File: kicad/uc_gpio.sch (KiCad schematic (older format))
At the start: 1 part, among them U1_? TMS320F28388DZWTS

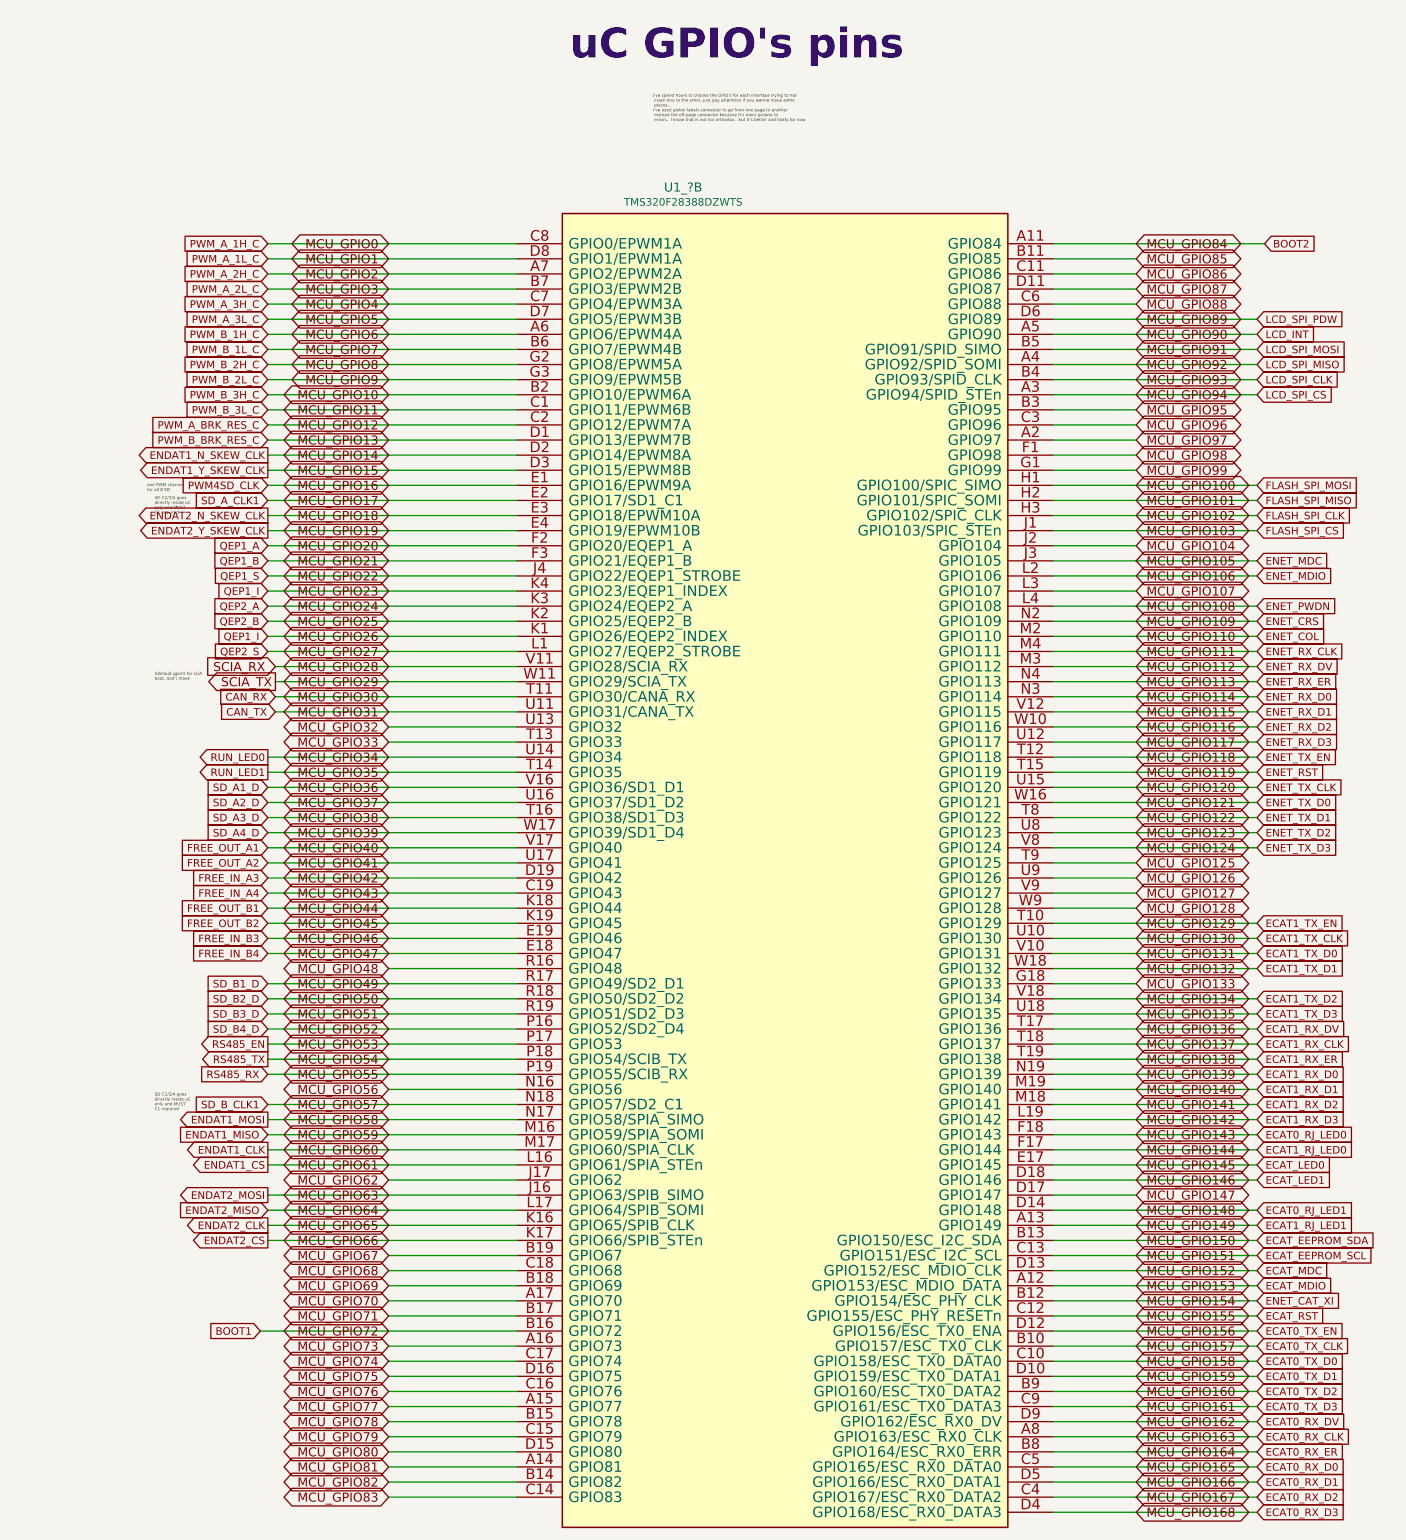
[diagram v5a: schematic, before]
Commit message: added 4 push buttons and more gpios on LCD connector
just to have more UI options. With those I'd manage graphics LCD plus 4
buttons, and charaveter LCD. or the embedded EVE graphic LCD
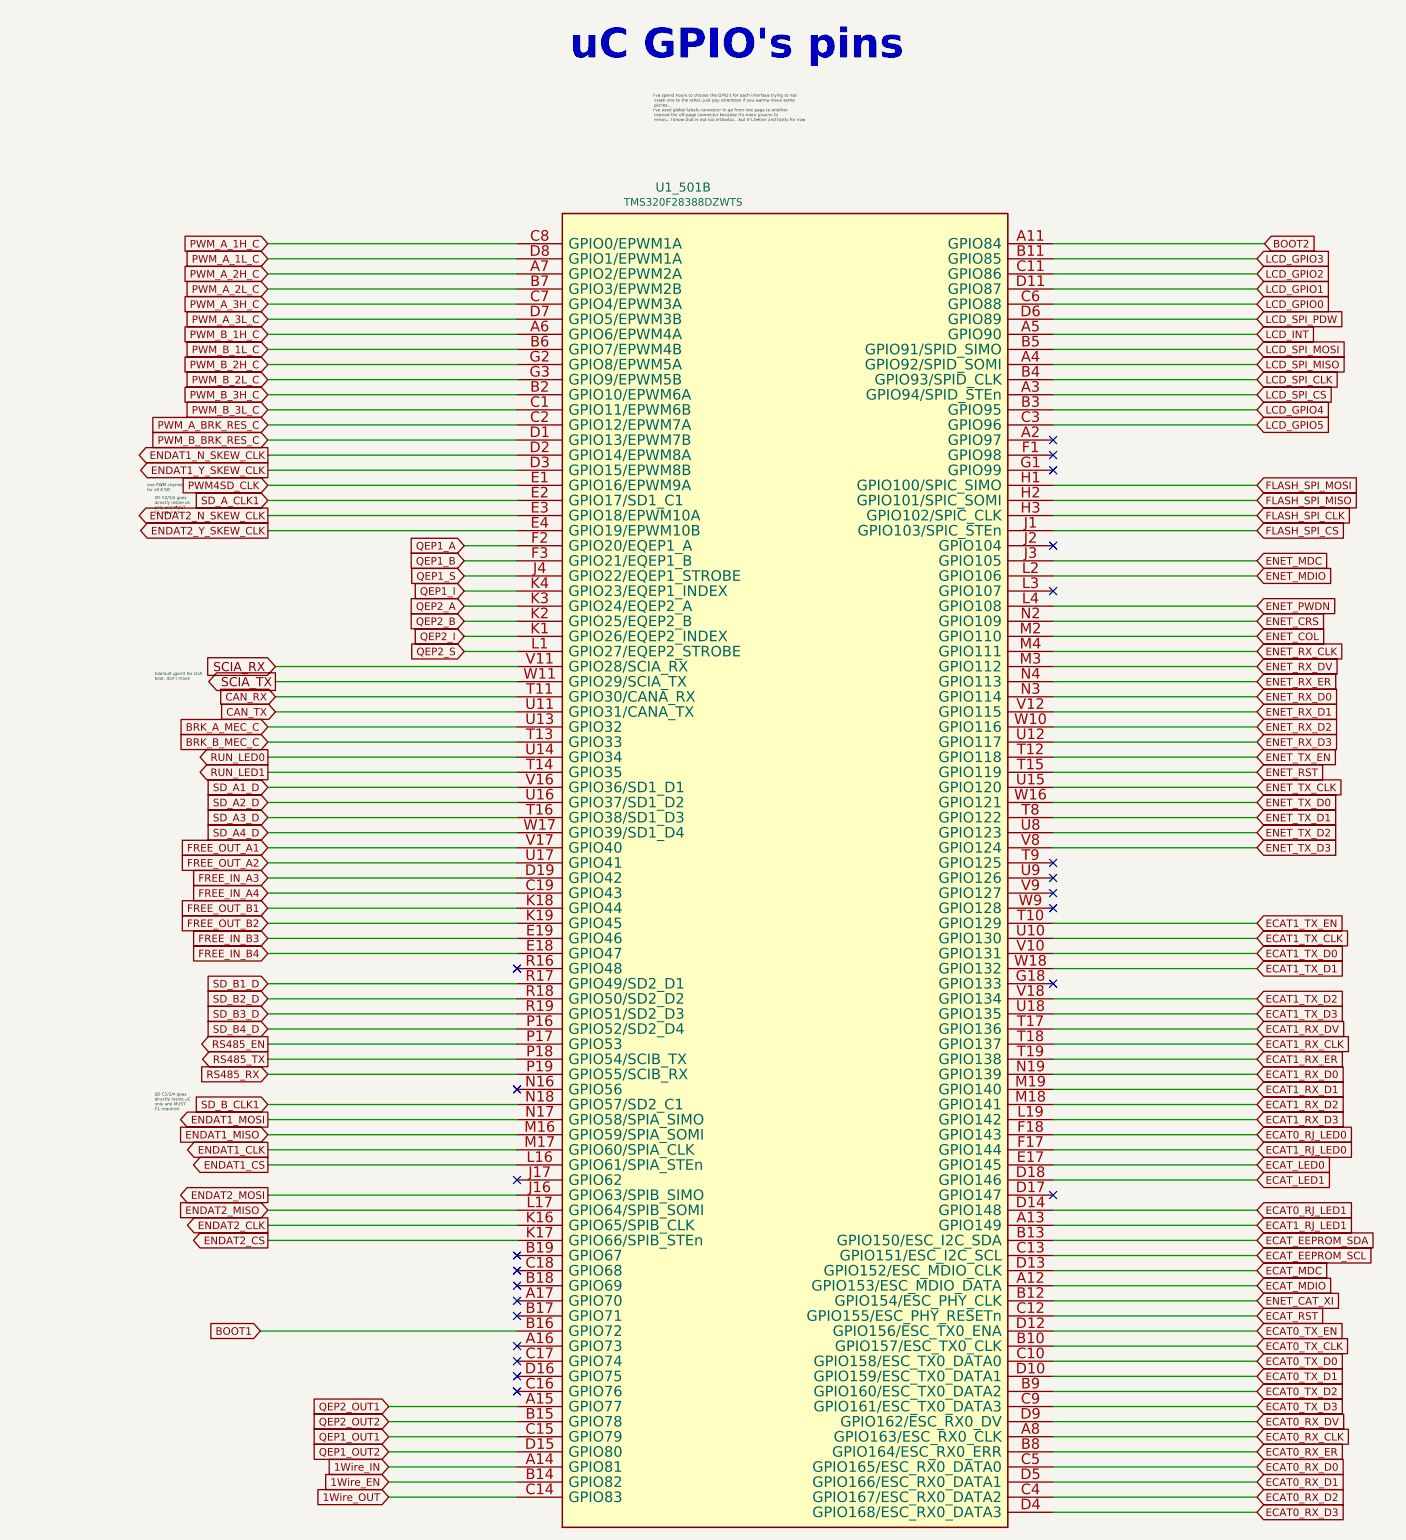
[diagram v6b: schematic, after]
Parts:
- gave numbers to parts that had none: 1
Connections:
- net MCU_GPIO0 renamed PWM_A_1H_C
- net MCU_GPIO1 renamed PWM_A_1L_C
- net MCU_GPIO10 renamed PWM_B_3H_C
- net MCU_GPIO104: no longer names the net of U1_501.J2 (GPIO104)
- net MCU_GPIO107: no longer names the net of U1_501.L3 (GPIO107)
- net MCU_GPIO11 renamed PWM_B_3L_C
- net MCU_GPIO12 renamed PWM_A_BRK_RES_C
- net MCU_GPIO125: no longer names the net of U1_501.T9 (GPIO125)
- net MCU_GPIO126: no longer names the net of U1_501.U9 (GPIO126)
- net MCU_GPIO127: no longer names the net of U1_501.V9 (GPIO127)
- net MCU_GPIO128: no longer names the net of U1_501.W9 (GPIO128)
- net MCU_GPIO13 renamed PWM_B_BRK_RES_C
- net MCU_GPIO133: no longer names the net of U1_501.G18 (GPIO133)
- net MCU_GPIO147: no longer names the net of U1_501.D17 (GPIO147)
- net MCU_GPIO16 renamed PWM4SD_CLK
- net MCU_GPIO17 renamed SD_A_CLK1
- net MCU_GPIO2 renamed PWM_A_2H_C
- net MCU_GPIO20 renamed QEP1_A
- net MCU_GPIO21 renamed QEP1_B
- net MCU_GPIO22 renamed QEP1_S
- net MCU_GPIO23 renamed QEP1_I
- net QEP1_I: no longer U1_501.K1 (GPIO26/EQEP2_INDEX)
- net MCU_GPIO24 renamed QEP2_A
- net MCU_GPIO25 renamed QEP2_B
- net MCU_GPIO27 renamed QEP2_S
- net MCU_GPIO28 renamed SCIA_RX
- net MCU_GPIO29 renamed SCIA_TX
- net MCU_GPIO3 renamed PWM_A_2L_C
- net MCU_GPIO32 renamed BRK_A_MEC_C
- net MCU_GPIO33 renamed BRK_B_MEC_C
- net MCU_GPIO34 renamed RUN_LED0
- net MCU_GPIO35 renamed RUN_LED1
- net MCU_GPIO36 renamed SD_A1_D
- net MCU_GPIO37 renamed SD_A2_D
- net MCU_GPIO38 renamed SD_A3_D
- net MCU_GPIO39 renamed SD_A4_D
- net MCU_GPIO4 renamed PWM_A_3H_C
- net MCU_GPIO48: no longer names the net of U1_501.R16 (GPIO48)
- net MCU_GPIO49 renamed SD_B1_D
- net MCU_GPIO5 renamed PWM_A_3L_C
- net MCU_GPIO50 renamed SD_B2_D
- net MCU_GPIO51 renamed SD_B3_D
- net MCU_GPIO52 renamed SD_B4_D
- net MCU_GPIO53 renamed RS485_EN
- net MCU_GPIO54 renamed RS485_TX
- net MCU_GPIO55 renamed RS485_RX
- net MCU_GPIO56: no longer names the net of U1_501.N16 (GPIO56)
- net MCU_GPIO57 renamed SD_B_CLK1
- net MCU_GPIO6 renamed PWM_B_1H_C
- net MCU_GPIO62: no longer names the net of U1_501.J17 (GPIO62)
- net MCU_GPIO67: no longer names the net of U1_501.B19 (GPIO67)
- net MCU_GPIO68: no longer names the net of U1_501.C18 (GPIO68)
- net MCU_GPIO69: no longer names the net of U1_501.B18 (GPIO69)
- net MCU_GPIO7 renamed PWM_B_1L_C
- net MCU_GPIO70: no longer names the net of U1_501.A17 (GPIO70)
- net MCU_GPIO71: no longer names the net of U1_501.B17 (GPIO71)
- net MCU_GPIO73: no longer names the net of U1_501.A16 (GPIO73)
- net MCU_GPIO74: no longer names the net of U1_501.C17 (GPIO74)
- net MCU_GPIO75: no longer names the net of U1_501.D16 (GPIO75)
- net MCU_GPIO76: no longer names the net of U1_501.C16 (GPIO76)
- net MCU_GPIO77 renamed QEP2_OUT1
- net MCU_GPIO78 renamed QEP2_OUT2
- net MCU_GPIO79 renamed QEP1_OUT1
- net MCU_GPIO8 renamed PWM_B_2H_C
- net MCU_GPIO80 renamed QEP1_OUT2
- net MCU_GPIO81 renamed 1Wire_IN
- net MCU_GPIO82 renamed 1Wire_EN
- net MCU_GPIO83 renamed 1Wire_OUT
- net MCU_GPIO85 renamed LCD_GPIO3
- net MCU_GPIO86 renamed LCD_GPIO2
- net MCU_GPIO87 renamed LCD_GPIO1
- net MCU_GPIO88 renamed LCD_GPIO0
- net MCU_GPIO9 renamed PWM_B_2L_C
- net MCU_GPIO95 renamed LCD_GPIO4
- net MCU_GPIO96 renamed LCD_GPIO5
- net MCU_GPIO97: no longer names the net of U1_501.A2 (GPIO97)
- net MCU_GPIO98: no longer names the net of U1_501.F1 (GPIO98)
- net MCU_GPIO99: no longer names the net of U1_501.G1 (GPIO99)
- new net QEP2_I: U1_501.K1 (GPIO26/EQEP2_INDEX)
- no-connect marks 0 -> 23

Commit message: begin PCB!! it's amess but IT IS
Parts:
- U1_501: footprint (none) -> servo:BGA337CP80_19X19_1600X1600X140B50N
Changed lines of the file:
@@
 F 0 "U1_501" H 5900 10873 60  0000 C CNN
 F 1 "TMS320F28388DZWTS" H 5900 10775 50  0000 C CNN
-F 2 "" H 5900 6300 50  0001 C CNN
+F 2 "servo:BGA337CP80_19X19_1600X1600X140B50N" H 5900 6300 50  0001 C CNN
 F 3 "../doc/datasheets/tms320f28388d_datasheet.pdf" H 5900 6300 50  0001 C CNN
 F 4 "TMS320F28388DZWTS" V 4300 3200 60  0001 C CNN "PartNumber"

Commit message: I've passed all footprin to layout BUT...
I've passed all, first glance... I need to confirm in details a lot of
things. The objetive for these is to have an aproximation of the size
I'll need to make the board.. then I choose the final detailed footprint
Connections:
- net SD_A1_D renamed SD_A1
- net SD_A2_D renamed SD_A2
- net SD_A3_D renamed SD_A3
- net SD_A4_D renamed SD_A4
- net SD_A_CLK1 renamed SD_A_CLK
- net SD_B1_D renamed SD_B1
- net SD_B2_D renamed SD_B2
- net SD_B3_D renamed SD_B3
- net SD_B4_D renamed SD_B4
- net SD_B_CLK1 renamed SD_B_CLK
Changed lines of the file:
@@
 $Descr A3 16535 11693
 encoding utf-8
-Sheet 14 18
+Sheet 14 19
 Title "gpio"
 Date "2020-01-09"
@@
 	3200 5000 4800 5000
 Text GLabel 3150 5700 0    50   Input ~ 0
-SD_A1_D
+SD_A1
 Text GLabel 3150 5800 0    50   Input ~ 0
-SD_A2_D
+SD_A2
 Text GLabel 3150 5900 0    50   Input ~ 0
-SD_A3_D
+SD_A3
 Text GLabel 3150 6000 0    50   Input ~ 0
-SD_A4_D
+SD_A4
 Text GLabel 3150 3300 0    50   Input ~ 0
 PWM_A_BRK_RES_C
@@
 PWM_B_BRK_RES_C
 Text GLabel 3150 7000 0    50   Input ~ 0
-SD_B1_D
+SD_B1
 Text GLabel 3150 7100 0    50   Input ~ 0
-SD_B2_D
+SD_B2
 Text GLabel 3150 7200 0    50   Input ~ 0
-SD_B3_D
+SD_B3
 Wire Wire Line
 	3150 7000 4800 7000
@@
 	3150 3800 4800 3800
 Text GLabel 3150 3800 0    50   Input ~ 0
-SD_A_CLK1
+SD_A_CLK
 Text GLabel 3150 3700 0    50   Input ~ 0
 PWM4SD_CLK
@@
 SD C2/3/4 goes\ndirectly inside uC\nonly and MUST  \nC1 required
 Text GLabel 3150 7800 0    50   Input ~ 0
-SD_B_CLK1
+SD_B_CLK
 Wire Wire Line
 	3150 7300 4800 7300
 Text GLabel 3150 7300 0    50   Input ~ 0
-SD_B4_D
+SD_B4
 Text GLabel 3150 7600 0    50   Input ~ 0
 RS485_RX
